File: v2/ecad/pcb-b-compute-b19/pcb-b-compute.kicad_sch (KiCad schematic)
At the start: 925 parts, among them Q1 CSD19532Q5B 100 V N-FET (4.6 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, Q10 2N7002: the changeover's comp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, Q101 BC857: LED_nPWR must be buffe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, Q102 2N7002, Q103 2N7002, Q104 2N7002, Q105 2N7002, Q106 2N7002 EMCON -> W_DISABLE1#, Q2 2N7002 expander -> switch res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, Q201 BC857: LED_nPWR must be buffe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, Q202 2N7002, Q203 2N7002, Q204 2N7002, Q205 2N7002, Q206 2N7002 EMCON -> W_DISABLE1#, Q207 2N7002 expander -> FULL_CARD_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, Q208 2N7002 expander -> RESET#, Q3 2N7002: a voted majority pull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, Q301 BC857: LED_nPWR must be buffe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, Q302 2N7002, Q303 2N7002, Q304 2N7002, Q305 2N7002, Q306 2N7002 EMCON -> W_DISABLE1#, Q4 2N7002: a voted majority pull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, Q5 2N7002: a voted majority pull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, T1 Pulse H5007NL 1000BASE-T magn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, U1 Microchip KSZ9897RTXI seven-p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, U10 TMP117AIDRVR board temperatur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, U101 Diodes PI7C9X2G404SL PCIe 2.0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, U102 TI TUSB8041IRGCR four-port US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, U103 AP64500SP-13 5 A buck, 3.3 V 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, U104 AP64500SP-13 5 A buck, 3.3 V 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, U105 TPS62933DRLR buck 1.0 V PCIe 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, U106 TPS62933DRLR buck 1.1 V hub c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, U107 USBLC6-2SC6, U109 TI TMUXHS4212 SuperSpeed 2:1 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, U11 Quectel LG290P03AAMD GNSS RTK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, U110 TI TS3USB221A USB2 2:1 host s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, U12 Ebyte E22-900M30S 1 W LoRa (S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, U13 Ebyte E72-2G4M20S1E CC2652P (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, U14 Ebyte E72-2G4M20S1E CC2652P (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, U15 CP2102N-A02-GQFN28 USB-UART b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, U16 CP2102N-A02-GQFN28 USB-UART b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, U17 CP2102N-A02-GQFN28 USB-UART b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, U18 CP2102N-A02-GQFN28 USB-UART b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, U19 SN74LVC08APWR quad AND: LimeS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, U20 SN74LVC08APWR quad AND: E72 r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, U201 Diodes PI7C9X2G404SL PCIe 2.0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, U202 TI TUSB8041IRGCR four-port US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, U203 AP64500SP-13 5 A buck, 3.3 V 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, U204 AP64500SP-13 5 A buck, 3.3 V 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, U205 TPS62933DRLR buck 1.0 V PCIe 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, U206 TPS62933DRLR buck 1.1 V hub c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, U207 USBLC6-2SC6, U209 TI TMUXHS4212 SuperSpeed 2:1 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, U21 TPS22810DRV, U210 TI TS3USB221A USB2 2:1 host s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, U22 TPS22810DRV, U23 TPS259631DDAR eFuse +5V_DEV -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, U24 TPS259631DDAR eFuse +5V_DEV -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, U25 AP63203WU-7 3.3 V 2 A buck: t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, U26 TPS62933DRLR buck 1.2 V Ether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, U27 AP2112K-2.5 LDO: the switch's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, U28 TPS2065CDBV, U29 USBLC6-2SC6, U3 TI TS3DV642A0RUAR HDMI 2:1 sw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, U301 Diodes PI7C9X2G404SL PCIe 2.0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, U302 TI TUSB8041IRGCR four-port US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, U303 AP64500SP-13 5 A buck, 3.3 V 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, U304 AP64500SP-13 5 A buck, 3.3 V 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, U305 TPS62933DRLR buck 1.0 V PCIe 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, U306 TPS62933DRLR buck 1.1 V hub c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, U307 USBLC6-2SC6, U309 TI TMUXHS4212 SuperSpeed 2:1 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, U30A Amphenol 10164227-1004A1RLF r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, U30B Amphenol 10164227-1004A1RLF r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, U310 TI TS3USB221A USB2 2:1 host s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, U31A Amphenol 10164227-1004A1RLF r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, U31B Amphenol 10164227-1004A1RLF r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

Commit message: fix(ecad): the six committed netlists came from schematics this tree does not hold [MESHSAT-862]
`sch_prov.py` records the sha256 of the schematic a netlist was generated from,
and on every one of the six boards it named a schematic that is not the one in
the repo: the netlists were regenerated and committed at 00:14 this morning
without their schematics, which are from 15 and 16 September. Board E is the
clearest case, its committed netlist carrying the SMCJ40A and the 100 V bulk
capacitor of the suppressor pass while its committed drawing still showed the
SMCJ33A they replaced.

Only board B tripped the timestamp guard, because only board B's schematic had
been rewritten (with identical content) after the netlist, so the contract gate
refused board B and passed five boards in the identical state. That is a guard
reading a proxy while the fact sits beside it.

- check_contracts compares the sidecar's schematic hash when there is one and
  keeps the mtime rule only for a netlist with no provenance. A rule holds both
  directions and fails on the pre-fix source ("a netlist generated from a
  schematic this tree does not hold was accepted because its mtime is older").
- the six schematics are regenerated by today's generators at each board's own
  declared phase, and each board's netlist was exported from the new schematic
  and compared with the committed one component by component and node by node:
  398/262, 931/1852, 194/144, 207/172, 161/118 and 56/39 components and nets
  agree on every node. No connectivity moved; what moved is the drawing, which
  had been left behind, and E's two part values, which the netlist already had.
  erc_gate PASS on all six.
- the contract gate on this tree now reads PASS of 72 where it read INCONCLUSIVE
  of 54 with 24 contracts unjudged, which is SCH-003 and INT-001 on six boards.

Suite 928 passing, 0 failing, 19 skipped.
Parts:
- removed C121, C223: 22u 10V X7R 1210, Capacitor_SMD:C_1210_3225Metric, symbol Device:C
- removed C218, C237, C238, C239, C240, C250, C266, C267, C268, C269, C289, C60: 100n, Capacitor_SMD:C_0603_1608Metric, symbol Device:C
- removed C229, C234: 10n, Capacitor_SMD:C_0603_1608Metric, symbol Device:C
- removed C231, C232, C249: 22u 6.3V, Capacitor_SMD:C_0805_2012Metric, symbol Device:C
- removed C277, C278, C281, C282, C375, C377, C381: 100n, Capacitor_SMD:C_0402_1005Metric, symbol Device:C
- removed C59: 4.7u, Capacitor_SMD:C_0805_2012Metric, symbol Device:C
- removed J_QMX: QMX USB lead (bank 2 hub, port 4): VBUS D- D+ GND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, Connector_PinHeader_2.54mm:PinHeader_1x04_P2.54mm_Vertical, symbol Connector_Generic:Conn_01x04
- removed L203, L204: 2.2uH XAL4020-222ME, Inductor_SMD:L_Coilcraft_XAL4020-XXX, symbol Device:L
- removed Q302: 2N7002, Package_TO_SOT_SMD:SOT-23, symbol Transistor_FET:2N7002
- removed R138, R245, R346: 10k, Resistor_SMD:R_0603_1608Metric, symbol Device:R
- removed R143: 90.9k 1%, Resistor_SMD:R_0603_1608Metric, symbol Device:R
- removed R150, R40: 1k, Resistor_SMD:R_0603_1608Metric, symbol Device:R
- removed R202: 31.6k 1%, Resistor_SMD:R_0603_1608Metric, symbol Device:R
- removed R205, R210: 22k, Resistor_SMD:R_0603_1608Metric, symbol Device:R
- removed R211, R477, R480, R481, R482, R483, R484: 100k, Resistor_SMD:R_0603_1608Metric, symbol Device:R
- removed R219, R320, R321: 5.1k, Resistor_SMD:R_0603_1608Metric, symbol Device:R
- removed R222, R324: 330, Resistor_SMD:R_0603_1608Metric, symbol Device:R
- removed R242: 9.53k 1%, Resistor_SMD:R_0603_1608Metric, symbol Device:R
- removed U303: AP64500SP-13 5 A buck, 3.3 V rail +3V3_S3A, Package_SO:SOIC-8-1EP_3.9x4.9mm_P1.27mm_EP2.29x3mm, symbol meshsat_ic:U303
- removed U34: USBLC6-2SC6, Package_TO_SOT_SMD:SOT-23-6, symbol Power_Protection:USBLC6-2SC6
- removed U40: AP2112K-3.3 LDO: the private 3.3 V of controller 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, Package_TO_SOT_SMD:SOT-23-5, symbol meshsat_ic:U40
- removed U62: SWD pads, controller C: 3V3 SWDIO SWCLK NRST GND, Connector_PinHeader_2.54mm:PinHeader_1x05_P2.54mm_Vertical, symbol meshsat_ic:U62
- removed U77: SN74LVC32APWR quad 2-input OR: the 2-of-3 majorit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, Package_SO:TSSOP-14_4.4x5mm_P0.65mm, symbol meshsat_ic:U77
- removed U8: ATECC608B-SSHDA-T secure element (I2C 0x60): keys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, Package_SO:SOIC-8_3.9x4.9mm_P1.27mm, symbol meshsat_ic:U8
- added C135, C241, C242, C243, C244, C245, C270, C271, C272, C273, C292, C294, C406, C475, C476, C477, C478, C479, C70: 100n, Capacitor_SMD:C_0603_1608Metric, symbol Device:C
- added C151, C152, C251, C252, C351, C352: 220n 16V (PCIe AC coupling, CM5 datasheet 2.3.1), Capacitor_SMD:C_0402_1005Metric, symbol Device:C
- added C157, C226, C227, C331: 22u 6.3V, Capacitor_SMD:C_0805_2012Metric, symbol Device:C
- added C159, C275, C279: 100n, Capacitor_SMD:C_0402_1005Metric, symbol Device:C
- added C212, C219: 22u 10V X7R 1210, Capacitor_SMD:C_1210_3225Metric, symbol Device:C
- added C225, C230: 10u, Capacitor_SMD:C_0805_2012Metric, symbol Device:C
- added C265: 18p, Capacitor_SMD:C_0402_1005Metric, symbol Device:C
- added C293: 1u, Capacitor_SMD:C_0603_1608Metric, symbol Device:C
- added C61: 10n, Capacitor_SMD:C_0603_1608Metric, symbol Device:C
- added J_FAN1: IP68 cooler fan of S1 (JST-SH 1.0): 5V GND TACHO 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, Connector_JST:JST_SH_BM04B-SRSS-TB_1x04-1MP_P1.00mm_Vertical, symbol Connector_Generic:Conn_01x04
- added L201, L202: 3.3uH XAL6030-332ME, Inductor_SMD:L_Coilcraft_XAL6060-XXX, symbol Device:L
- added LED23, LED33: green card link (PORTSTATUS1), LED_SMD:LED_0603_1608Metric, symbol Device:LED
- added LED26, LED36: green ACT (LED_nACT sinks), LED_SMD:LED_0603_1608Metric, symbol Device:LED
- added LED31: green 5 V S3, LED_SMD:LED_0603_1608Metric, symbol Device:LED
- added Q206: 2N7002 EMCON -> W_DISABLE1#, Package_TO_SOT_SMD:SOT-23, symbol Transistor_FET:2N7002
- added R208: 10k 1%, Resistor_SMD:R_0603_1608Metric, symbol Device:R
- added R214: 40.2k 1%, Resistor_SMD:R_0603_1608Metric, symbol Device:R
- added R216: 26.7k 1%, Resistor_SMD:R_0603_1608Metric, symbol Device:R
- added R230, R330: 1k, Resistor_SMD:R_0603_1608Metric, symbol Device:R
- added R251, R349, R351, R44: 10k, Resistor_SMD:R_0603_1608Metric, symbol Device:R
- added R305: 22k, Resistor_SMD:R_0603_1608Metric, symbol Device:R
- added R328: 330, Resistor_SMD:R_0603_1608Metric, symbol Device:R
- added R43: 301R 1% (ILM: 3.0 A), Resistor_SMD:R_0603_1608Metric, symbol Device:R
- added R478: 100k, Resistor_SMD:R_0603_1608Metric, symbol Device:R
- added U19: SN74LVC08APWR quad AND: LimeSDR (hub port power A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, Package_SO:TSSOP-14_4.4x5mm_P0.65mm, symbol meshsat_ic:U19
- added U29: USBLC6-2SC6, Package_TO_SOT_SMD:SOT-23-6, symbol Power_Protection:USBLC6-2SC6
- added U63: TCAN334D CAN-FD transceiver, controller C on hear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, Package_SO:SOIC-8_3.9x4.9mm_P1.27mm, symbol meshsat_ic:U63
- added U78: SN74LVC32APWR quad 2-input OR: the 2-of-3 majorit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, Package_SO:TSSOP-14_4.4x5mm_P0.65mm, symbol meshsat_ic:U78
- C114: renamed from C157; value 22u 6.3V -> 22u 10V X7R 1210; footprint Capacitor_SMD:C_0805_2012Metric -> Capacitor_SMD:C_1210_3225Metric
- C121: renamed from C135; value 100n -> 22u 10V X7R 1210; footprint Capacitor_SMD:C_0603_1608Metric -> Capacitor_SMD:C_1210_3225Metric
- C218: renamed from R207; value 31.6k 1% -> 100n; footprint Resistor_SMD:R_0603_1608Metric -> Capacitor_SMD:C_0603_1608Metric; symbol Device:R -> Device:C
- C223: renamed from C247; value 10u -> 22u 10V X7R 1210; footprint Capacitor_SMD:C_0805_2012Metric -> Capacitor_SMD:C_1210_3225Metric
- C229: renamed from C225; value 10u -> 10n; footprint Capacitor_SMD:C_0805_2012Metric -> Capacitor_SMD:C_0603_1608Metric
- C231: renamed from C270; value 100n -> 22u 6.3V; footprint Capacitor_SMD:C_0603_1608Metric -> Capacitor_SMD:C_0805_2012Metric
- C232: renamed from C271; value 100n -> 22u 6.3V; footprint Capacitor_SMD:C_0603_1608Metric -> Capacitor_SMD:C_0805_2012Metric
- C234: renamed from C230; value 10u -> 10n; footprint Capacitor_SMD:C_0805_2012Metric -> Capacitor_SMD:C_0603_1608Metric
- C237: renamed from C226; value 22u 6.3V -> 100n; footprint Capacitor_SMD:C_0805_2012Metric -> Capacitor_SMD:C_0603_1608Metric
- C238: renamed from C227; value 22u 6.3V -> 100n; footprint Capacitor_SMD:C_0805_2012Metric -> Capacitor_SMD:C_0603_1608Metric
- C247: renamed from C243; value 100n -> 10u; footprint Capacitor_SMD:C_0603_1608Metric -> Capacitor_SMD:C_0805_2012Metric
- C249: renamed from C244; value 100n -> 22u 6.3V; footprint Capacitor_SMD:C_0603_1608Metric -> Capacitor_SMD:C_0805_2012Metric
- C269: renamed from C293; value 1u -> 100n
- C274: renamed from C294; value 100n -> 10u; footprint Capacitor_SMD:C_0603_1608Metric -> Capacitor_SMD:C_0805_2012Metric
- C276: renamed from LED26; value green ACT (LED_nACT sinks) -> 100n; footprint LED_SMD:LED_0603_1608Metric -> Capacitor_SMD:C_0402_1005Metric; symbol Device:LED -> Device:C; LCSC C12624 -> (none)
- C280: renamed from R251; value 10k -> 100n; footprint Resistor_SMD:R_0603_1608Metric -> Capacitor_SMD:C_0402_1005Metric; symbol Device:R -> Device:C
- C289: renamed from Q206; value 2N7002 EMCON -> W_DISABLE1# -> 100n; footprint Package_TO_SOT_SMD:SOT-23 -> Capacitor_SMD:C_0603_1608Metric; symbol Transistor_FET:2N7002 -> Device:C; LCSC C8545 -> (none)
- C375: renamed from R349; value 10k -> 100n; footprint Resistor_SMD:R_0603_1608Metric -> Capacitor_SMD:C_0402_1005Metric; symbol Device:R -> Device:C
- C377: renamed from LED36; value green ACT (LED_nACT sinks) -> 100n; footprint LED_SMD:LED_0603_1608Metric -> Capacitor_SMD:C_0402_1005Metric; symbol Device:LED -> Device:C; LCSC C12624 -> (none)
- C381: renamed from R351; value 10k -> 100n; footprint Resistor_SMD:R_0603_1608Metric -> Capacitor_SMD:C_0402_1005Metric; symbol Device:R -> Device:C
- C59: renamed from R44; value 10k -> 4.7u; footprint Resistor_SMD:R_0603_1608Metric -> Capacitor_SMD:C_0805_2012Metric; symbol Device:R -> Device:C
- C60: renamed from R43; value 301R 1% (ILM: 3.0 A) -> 100n; footprint Resistor_SMD:R_0603_1608Metric -> Capacitor_SMD:C_0603_1608Metric; symbol Device:R -> Device:C
- D101, D201, D301: value SMBJ5.0A -> SMBJ6.0A (6.0 V standoff on the 5.1 V slot rail); LCSC (none) -> C83270
- J_QMX: renamed from U19; value SN74LVC08APWR quad AND: LimeSDR (hub port power AND EMCON AND software), RockBLOCK (EMCON AND software), LoRa (EMCON AN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 -> QMX USB lead (bank 2 hub, port 4): VBUS D- D+ GND; pigtail to the unit's USB-C; footprint Package_SO:TSSOP-14_4.4x5mm_P0.65mm -> Connector_PinHeader_2.54mm:PinHeader_1x04_P2.54mm_Vertical; symbol meshsat_ic:U19 -> Connector_Generic:Conn_01x04; LCSC C465737 -> (none)
- L203: renamed from R214; value 40.2k 1% -> 2.2uH XAL4020-222ME; footprint Resistor_SMD:R_0603_1608Metric -> Inductor_SMD:L_Coilcraft_XAL4020-XXX; symbol Device:R -> Device:L
- L204: renamed from R216; value 26.7k 1% -> 2.2uH XAL4020-222ME; footprint Resistor_SMD:R_0603_1608Metric -> Inductor_SMD:L_Coilcraft_XAL4020-XXX; symbol Device:R -> Device:L
- Q302: renamed from LED31; value green 5 V S3 -> 2N7002; footprint LED_SMD:LED_0603_1608Metric -> Package_TO_SOT_SMD:SOT-23; symbol Device:LED -> Transistor_FET:2N7002; LCSC C12624 -> C8545
- R138: renamed from C114; value 22u 10V X7R 1210 -> 10k; footprint Capacitor_SMD:C_1210_3225Metric -> Resistor_SMD:R_0603_1608Metric; symbol Device:C -> Device:R
- R143: renamed from C159; value 100n -> 90.9k 1%; footprint Capacitor_SMD:C_0402_1005Metric -> Resistor_SMD:R_0603_1608Metric; symbol Device:C -> Device:R
- R150: renamed from J_FAN1; value IP68 cooler fan of S1 (JST-SH 1.0): 5V GND TACHO PWM -> 1k; footprint Connector_JST:JST_SH_BM04B-SRSS-TB_1x04-1MP_P1.00mm_Vertical -> Resistor_SMD:R_0603_1608Metric; symbol Connector_Generic:Conn_01x04 -> Device:R; LCSC C160390 -> (none)
- R202: renamed from L201; value 3.3uH XAL6030-332ME -> 31.6k 1%; footprint Inductor_SMD:L_Coilcraft_XAL6060-XXX -> Resistor_SMD:R_0603_1608Metric; symbol Device:L -> Device:R
- R205: renamed from C212; value 22u 10V X7R 1210 -> 22k; footprint Capacitor_SMD:C_1210_3225Metric -> Resistor_SMD:R_0603_1608Metric; symbol Device:C -> Device:R
- R207: renamed from L202; value 3.3uH XAL6030-332ME -> 31.6k 1%; footprint Inductor_SMD:L_Coilcraft_XAL6060-XXX -> Resistor_SMD:R_0603_1608Metric; symbol Device:L -> Device:R
- R210: renamed from C219; value 22u 10V X7R 1210 -> 22k; footprint Capacitor_SMD:C_1210_3225Metric -> Resistor_SMD:R_0603_1608Metric; symbol Device:C -> Device:R
- R211: renamed from R208; value 10k 1% -> 100k
- R219: renamed from LED23; value green card link (PORTSTATUS1) -> 5.1k; footprint LED_SMD:LED_0603_1608Metric -> Resistor_SMD:R_0603_1608Metric; symbol Device:LED -> Device:R; LCSC C12624 -> (none)
- R222: renamed from R230; value 1k -> 330
- R242: renamed from C274; value 10u -> 9.53k 1%; footprint Capacitor_SMD:C_0805_2012Metric -> Resistor_SMD:R_0603_1608Metric; symbol Device:C -> Device:R
- R245: renamed from C265; value 18p -> 10k; footprint Capacitor_SMD:C_0402_1005Metric -> Resistor_SMD:R_0603_1608Metric; symbol Device:C -> Device:R
- R320: renamed from R328; value 330 -> 5.1k
- R321: renamed from LED33; value green card link (PORTSTATUS1) -> 5.1k; footprint LED_SMD:LED_0603_1608Metric -> Resistor_SMD:R_0603_1608Metric; symbol Device:LED -> Device:R; LCSC C12624 -> (none)
- R324: renamed from R330; value 1k -> 330
- R346: renamed from C331; value 22u 6.3V -> 10k; footprint Capacitor_SMD:C_0805_2012Metric -> Resistor_SMD:R_0603_1608Metric; symbol Device:C -> Device:R
- R40: renamed from C61; value 10n -> 1k; footprint Capacitor_SMD:C_0603_1608Metric -> Resistor_SMD:R_0603_1608Metric; symbol Device:C -> Device:R
- R480: renamed from C475; value 100n -> 100k; footprint Capacitor_SMD:C_0603_1608Metric -> Resistor_SMD:R_0603_1608Metric; symbol Device:C -> Device:R
- R481: renamed from C476; value 100n -> 100k; footprint Capacitor_SMD:C_0603_1608Metric -> Resistor_SMD:R_0603_1608Metric; symbol Device:C -> Device:R
- R482: renamed from C477; value 100n -> 100k; footprint Capacitor_SMD:C_0603_1608Metric -> Resistor_SMD:R_0603_1608Metric; symbol Device:C -> Device:R
- R483: renamed from C479; value 100n -> 100k; footprint Capacitor_SMD:C_0603_1608Metric -> Resistor_SMD:R_0603_1608Metric; symbol Device:C -> Device:R
- R484: renamed from C478; value 100n -> 100k; footprint Capacitor_SMD:C_0603_1608Metric -> Resistor_SMD:R_0603_1608Metric; symbol Device:C -> Device:R
- U303: renamed from R305; value 22k -> AP64500SP-13 5 A buck, 3.3 V rail +3V3_S3A; footprint Resistor_SMD:R_0603_1608Metric -> Package_SO:SOIC-8-1EP_3.9x4.9mm_P1.27mm_EP2.29x3mm; symbol Device:R -> meshsat_ic:U303; LCSC (none) -> C2070920
- U40: renamed from C406; value 100n -> AP2112K-3.3 LDO: the private 3.3 V of controller A, its own branch off the device rail; footprint Capacitor_SMD:C_0603_1608Metric -> Package_TO_SOT_SMD:SOT-23-5; symbol Device:C -> meshsat_ic:U40
- U62: renamed from U63; value TCAN334D CAN-FD transceiver, controller C on heartbeat fabric A -> SWD pads, controller C: 3V3 SWDIO SWCLK NRST GND; footprint Package_SO:SOIC-8_3.9x4.9mm_P1.27mm -> Connector_PinHeader_2.54mm:PinHeader_1x05_P2.54mm_Vertical; symbol meshsat_ic:U63 -> meshsat_ic:U62; LCSC C2871143 -> (none)
- U77: renamed from U78; symbol meshsat_ic:U78 -> meshsat_ic:U77
- U8: renamed from C70; value 100n -> ATECC608B-SSHDA-T secure element (I2C 0x60): keys behind ZEROIZE; footprint Capacitor_SMD:C_0603_1608Metric -> Package_SO:SOIC-8_3.9x4.9mm_P1.27mm; symbol Device:C -> meshsat_ic:U8; LCSC (none) -> C1518769
- renumbered C241 to C239, C242 to C240, C245 to C250, C272 to C266, C273 to C267, C292 to C268, C276 to C277, C275 to C278, C280 to C281, C279 to C282, R478 to R477, U29 to U34
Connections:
- net +1V0_S2: now also L203.2, C226.1, C227.1, C241.1, C242.1, C243.1, C244.1, C245.1; no longer C237.1, C238.1, C239.1, C240.1, C247.1, C249.1, C250.1
- net +1V1_S2: now also C231.1, C232.1, C266.1, C267.1, C268.1, C269.1, C274.1, L204.2; no longer R242.1
- net +1V1_S3: now also C331.1; no longer R346.1
- net +3V3_CM2: now also R211.1, R251.2; no longer C280.2
- net +3V3_CM3: now also Q302.1 (G), R351.2; no longer C381.2
- net +3V3_DEV: now also R245.2, R346.2, U8.8 (+3V3_DEV), C270.1, C271.1, C272.1, C273.1, C292.1, C293.1, C294.1, C475.1, C476.1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; no longer C231.1, C232.1, C266.1, C267.1, C268.1, C269.1, C274.1, C59.2, J_QMX.14 (+3V3_DEV), R480.1, R481.1, R482.1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
- net +3V3_IOCA: now also U40.5 (+3V3_IOCA), C406.1; no longer U40.1
- net +3V3_IOCC: now also U62.1 (+3V3_IOCC), U63.3 (+3V3_IOCC); no longer U62.3 (+3V3_IOCC)
- net +3V3_S1A: now also R138.2, C157.1; no longer R138.1
- net +3V3_S1B: now also C135.1
- net +3V3_S2A: now also R202.1, L201.2, Q206.1 (G); no longer C289.1 (G), R202.2
- net +3V3_S2B: now also C237.1, C238.1, C239.1, C240.1, C247.1, C249.1, C250.1, R207.1, R219.2, L202.2, R230.1; no longer C218.1, R207.2, R222.1
- net +3V3_S3B: now also R320.2, R321.2, R330.1; no longer R324.1
- net +5V_CAM: now also U34.5 (VBUS)
- net +5V_DEV: now also R143.1, U40.1 (+5V_DEV), U40.3 (+5V_DEV), C230.1; no longer C234.1
- net +5V_S1: now also J_FAN1.1 (Pin_1); no longer R150.1 (Pin_1)
- net +5V_S2: now also C212.1, C219.1, C225.1; no longer C229.1, R205.1, R210.1
- net +5V_S3: now also U303.2 (+5V_S3)
- net 5G_W_DIS_n: now also Q206.2 (S); no longer C289.2 (S)
- net BANK1_UPRX_P: now also C159.1; no longer R143.1
- net BSEL3: now also U77.6 (BSEL3)
- net CAM_DM: now also U34.3 (I/O2), U34.4 (I/O2)
- net CAM_DP: now also U34.1 (I/O1), U34.6 (I/O1)
- net CANH_A: now also U63.7 (CANH_A); no longer U62.7 (CANH_A)
- net CANL_A: now also U63.6 (CANL_A); no longer U62.6 (CANL_A)
- net E22_EN: now also U19.11 (E22_EN); no longer J_QMX.11 (E22_EN)
- net EMCON_HW: now also Q206.3 (D), U19.1 (EMCON_HW), U19.12 (EMCON_HW), U19.9 (EMCON_HW); no longer C289.3 (D), J_QMX.1 (EMCON_HW), J_QMX.12 (EMCON_HW), J_QMX.9 (EMCON_HW)
- net EN33_S2: now also R211.2
- net ETH2_P0_N: now also C276.1; no longer C277.1
- net ETH2_P0_P: now also C275.1; no longer C278.1
- net ETH2_P1_N: now also C278.1
- net ETH2_P1_P: now also C277.1
- net ETH2_P2_N: now also C280.1; no longer C281.1
- net ETH2_P2_P: now also C279.1; no longer C282.1
- net ETH2_P3_N: now also C282.1
- net ETH2_P3_P: now also C281.1
- net ETH3_P0_P: now also C375.1
- net ETH3_P1_P: now also C377.1
- net ETH3_P3_P: now also C381.1
- net FAN_PWM1: now also J_FAN1.4 (Pin_4); no longer R150.4 (Pin_4)
- net FAN_PWM2: now also R251.1; no longer C280.1
- net FAN_PWM3: now also R351.1; no longer C381.1
- net FAN_TACHO1: now also J_FAN1.3 (Pin_3); no longer R150.3 (Pin_3)
- net GND: now also C289.2, C59.2, J_QMX.4 (Pin_4), R222.2, R324.2, U303.7 (GND), U303.9 (GND), U62.5 (GND), U8.4 (GND), C135.2, C157.2, C212.2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; no longer J_QMX.7 (GND), L203.2, L204.2, Q302.1 (K), R138.2, R150.2 (Pin_2), R205.2, R210.2, R211.2, R245.2, R320.2, R346.2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
- net HUB1_VBUS: now also R143.2
- net HUB2_R1: now also R242.1
- net HUB2_SMBUS_n: now also R245.1
- net HUB2_XO: now also C265.1; no longer R245.1
- net HUB3_PWRPOL: now also R346.1
- net HUBRST1_AB: now also U77.10 (HUBRST1_AB)
- net HUBRST1_BC: now also U77.9 (HUBRST1_BC)
- net HUBRST1_CA: now also U77.12 (HUBRST1_CA)
- net HUBRST1_O1: now also U77.13 (HUBRST1_O1), U77.8 (HUBRST1_O1)
- net HUBRST1_VOTE: now also R477.1, U77.11 (HUBRST1_VOTE)
- net HUBRST2_AB: now also U78.1 (HUBRST2_AB); no longer U77.1 (HUBRST2_AB)
- net HUBRST2_BC: now also U78.2 (HUBRST2_BC); no longer U77.2 (HUBRST2_BC)
- net HUBRST2_CA: now also U78.5 (HUBRST2_CA); no longer U77.5 (HUBRST2_CA)
- net HUBRST2_O1: now also U78.3 (HUBRST2_O1), U78.4 (HUBRST2_O1); no longer U77.3 (HUBRST2_O1), U77.4 (HUBRST2_O1)
- net HUBRST2_VOTE: now also R478.1, U78.6 (HUBRST2_VOTE); no longer R477.1, U77.6 (HUBRST2_VOTE)
- net HUBRST3_AB: now also U78.10 (HUBRST3_AB); no longer U77.10 (HUBRST3_AB)
- net HUBRST3_BC: now also U78.9 (HUBRST3_BC); no longer U77.9 (HUBRST3_BC)
- net HUBRST3_CA: now also U78.12 (HUBRST3_CA); no longer U77.12 (HUBRST3_CA)
- net HUBRST3_O1: now also U78.13 (HUBRST3_O1), U78.8 (HUBRST3_O1); no longer U77.13 (HUBRST3_O1), U77.8 (HUBRST3_O1)
- net HUBRST3_VOTE: now also U78.11 (HUBRST3_VOTE); no longer U77.11 (HUBRST3_VOTE)
- new net PCIE1_RXSW_N: C152.1, U101.123 (PETN0)
- new net PCIE1_RXSW_P: C151.1, U101.124 (PETP0)
- new net PCIE2_RXSW_N: C252.1, U201.123 (PETN0)
- new net PCIE2_RXSW_P: C251.1, U201.124 (PETP0)
- new net PCIE3_RXSW_N: C352.1, U301.123 (PETN0)
- new net PCIE3_RXSW_P: C351.1, U301.124 (PETP0)
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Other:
- note added: "220n 16V"
- note added: "SMBJ6.0A"
- note added: "page 1 of 37 MeshSat field kit V2, CERN-OHL-S-2.0 PROTOTYPE, nothing built 2026-09-17"
- note added: "page 10 of 37 MeshSat field kit V2, CERN-OHL-S-2.0 PROTOTYPE, nothing built 2026-09-17"
- note added: "page 11 of 37 MeshSat field kit V2, CERN-OHL-S-2.0 PROTOTYPE, nothing built 2026-09-17"
- note added: "page 12 of 37 MeshSat field kit V2, CERN-OHL-S-2.0 PROTOTYPE, nothing built 2026-09-17"
- note added: "page 13 of 37 MeshSat field kit V2, CERN-OHL-S-2.0 PROTOTYPE, nothing built 2026-09-17"
- note added: "page 14 of 37 MeshSat field kit V2, CERN-OHL-S-2.0 PROTOTYPE, nothing built 2026-09-17"
- note added: "page 15 of 37 MeshSat field kit V2, CERN-OHL-S-2.0 PROTOTYPE, nothing built 2026-09-17"
- note added: "page 16 of 37 MeshSat field kit V2, CERN-OHL-S-2.0 PROTOTYPE, nothing built 2026-09-17"
- note added: "page 17 of 37 MeshSat field kit V2, CERN-OHL-S-2.0 PROTOTYPE, nothing built 2026-09-17"
- note added: "page 18 of 37 MeshSat field kit V2, CERN-OHL-S-2.0 PROTOTYPE, nothing built 2026-09-17"
- note added: "page 19 of 37 MeshSat field kit V2, CERN-OHL-S-2.0 PROTOTYPE, nothing built 2026-09-17"
- note added: "page 2 of 37 MeshSat field kit V2, CERN-OHL-S-2.0 PROTOTYPE, nothing built 2026-09-17"
- note added: "page 20 of 37 MeshSat field kit V2, CERN-OHL-S-2.0 PROTOTYPE, nothing built 2026-09-17"
- note added: "page 21 of 37 MeshSat field kit V2, CERN-OHL-S-2.0 PROTOTYPE, nothing built 2026-09-17"
- note added: "page 22 of 37 MeshSat field kit V2, CERN-OHL-S-2.0 PROTOTYPE, nothing built 2026-09-17"
- note added: "page 23 of 37 MeshSat field kit V2, CERN-OHL-S-2.0 PROTOTYPE, nothing built 2026-09-17"
- note added: "page 24 of 37 MeshSat field kit V2, CERN-OHL-S-2.0 PROTOTYPE, nothing built 2026-09-17"
- note added: "page 25 of 37 MeshSat field kit V2, CERN-OHL-S-2.0 PROTOTYPE, nothing built 2026-09-17"
- note added: "page 26 of 37 MeshSat field kit V2, CERN-OHL-S-2.0 PROTOTYPE, nothing built 2026-09-17"
- note added: "page 27 of 37 MeshSat field kit V2, CERN-OHL-S-2.0 PROTOTYPE, nothing built 2026-09-17"
- note added: "page 28 of 37 MeshSat field kit V2, CERN-OHL-S-2.0 PROTOTYPE, nothing built 2026-09-17"
- note added: "page 29 of 37 MeshSat field kit V2, CERN-OHL-S-2.0 PROTOTYPE, nothing built 2026-09-17"
- note added: "page 3 of 37 MeshSat field kit V2, CERN-OHL-S-2.0 PROTOTYPE, nothing built 2026-09-17"
- note added: "page 30 of 37 MeshSat field kit V2, CERN-OHL-S-2.0 PROTOTYPE, nothing built 2026-09-17"
- note added: "page 31 of 37 MeshSat field kit V2, CERN-OHL-S-2.0 PROTOTYPE, nothing built 2026-09-17"
- note added: "page 32 of 37 MeshSat field kit V2, CERN-OHL-S-2.0 PROTOTYPE, nothing built 2026-09-17"
- note added: "page 33 of 37 MeshSat field kit V2, CERN-OHL-S-2.0 PROTOTYPE, nothing built 2026-09-17"
- note added: "page 34 of 37 MeshSat field kit V2, CERN-OHL-S-2.0 PROTOTYPE, nothing built 2026-09-17"
- note added: "page 35 of 37 MeshSat field kit V2, CERN-OHL-S-2.0 PROTOTYPE, nothing built 2026-09-17"
- note added: "page 36 of 37 MeshSat field kit V2, CERN-OHL-S-2.0 PROTOTYPE, nothing built 2026-09-17"
- note added: "page 37 of 37 MeshSat field kit V2, CERN-OHL-S-2.0 PROTOTYPE, nothing built 2026-09-17"
- note added: "page 4 of 37 MeshSat field kit V2, CERN-OHL-S-2.0 PROTOTYPE, nothing built 2026-09-17"
- note added: "page 5 of 37 MeshSat field kit V2, CERN-OHL-S-2.0 PROTOTYPE, nothing built 2026-09-17"
- note added: "page 6 of 37 MeshSat field kit V2, CERN-OHL-S-2.0 PROTOTYPE, nothing built 2026-09-17"
- note added: "page 7 of 37 MeshSat field kit V2, CERN-OHL-S-2.0 PROTOTYPE, nothing built 2026-09-17"
- note added: "page 8 of 37 MeshSat field kit V2, CERN-OHL-S-2.0 PROTOTYPE, nothing built 2026-09-17"
- note added: "page 9 of 37 MeshSat field kit V2, CERN-OHL-S-2.0 PROTOTYPE, nothing built 2026-09-17"
- note removed: "page 1 of 37 MeshSat field kit V2, CERN-OHL-S-2.0 PROTOTYPE, nothing built 2026-09-15"
- note removed: "page 10 of 37 MeshSat field kit V2, CERN-OHL-S-2.0 PROTOTYPE, nothing built 2026-09-15"
- note removed: "page 11 of 37 MeshSat field kit V2, CERN-OHL-S-2.0 PROTOTYPE, nothing built 2026-09-15"
- note removed: "page 12 of 37 MeshSat field kit V2, CERN-OHL-S-2.0 PROTOTYPE, nothing built 2026-09-15"
- note removed: "page 13 of 37 MeshSat field kit V2, CERN-OHL-S-2.0 PROTOTYPE, nothing built 2026-09-15"
- note removed: "page 14 of 37 MeshSat field kit V2, CERN-OHL-S-2.0 PROTOTYPE, nothing built 2026-09-15"
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
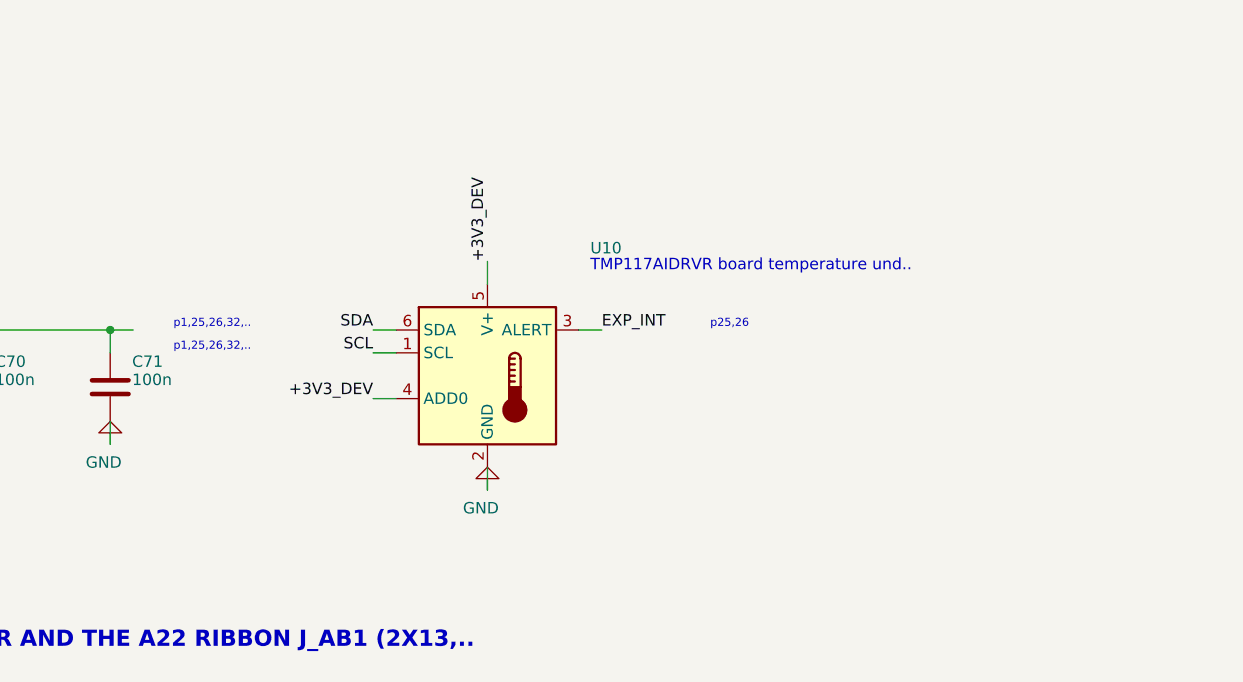
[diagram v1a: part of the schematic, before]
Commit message: fix(ecad): the six netlists regenerated under tonight's engine, with their provenance committed beside them [MESHSAT-862]
kisch.py changed tonight (every map judged against its land and its symbol), so
every committed netlist's sidecar named an older generator and the contract gate
refused to judge the set. Regenerated on the hub at each board's declared phase:
A, C, D and P come back IDENTICAL on every connectivity line (2316, 1067, 1193,
295); B differs by U10's seven pins, E by Q7's five, which are the two design
corrections of 32.219. Board E's board now reads 4 of 818 comparisons behind its
design (Q7) and board B19's 13 of 6735 (U10 and the twelve PCIe receive nets B21
carries), both SCH-002 FAIL and both true.

The sidecars were gitignored with the rest of out/, so every clone had six
netlists with no identity and the gate fell back to the mtime rule that refused one
board and passed five in the identical state this morning; they are force-added and
a rule keeps them beside their netlists. check_contracts reads PASS of 72 on this
tree. Readiness 58.1 percent verified, 11.1 failed, 30.8 inconclusive of 334.
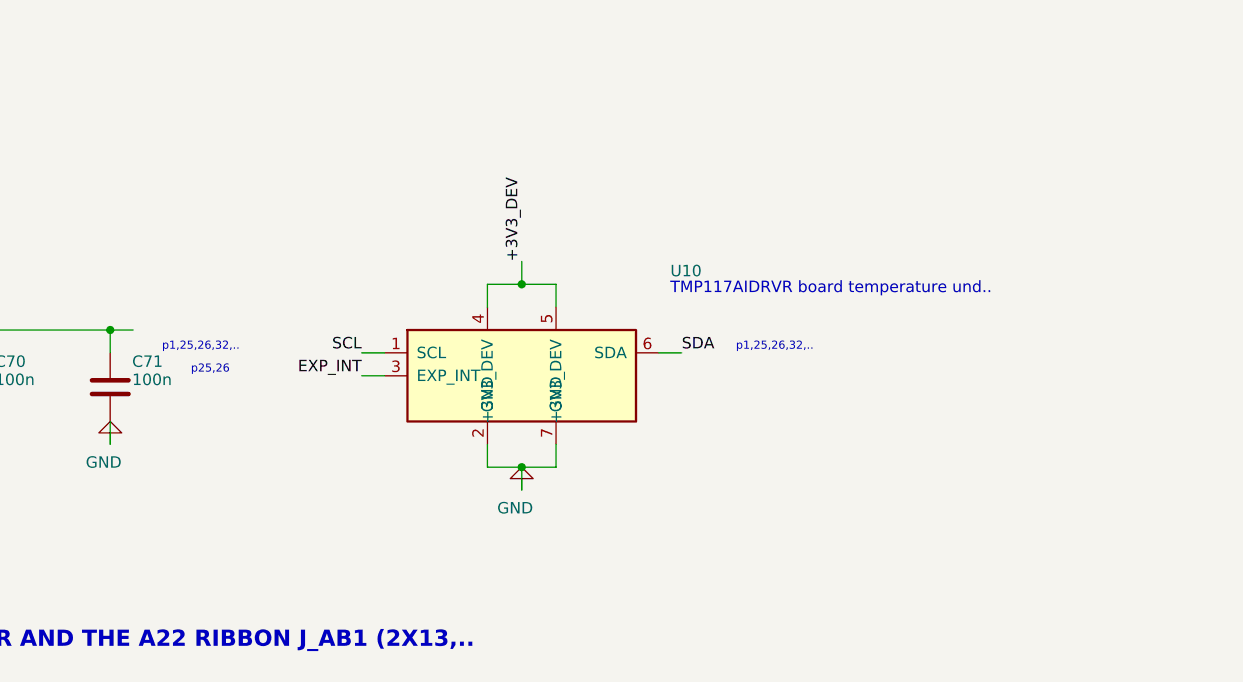
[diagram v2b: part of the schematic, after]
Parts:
- removed R483: 100k, Resistor_SMD:R_0603_1608Metric, symbol Device:R
- added C470: 100n, Capacitor_SMD:C_0603_1608Metric, symbol Device:C
- R483: renamed from C470; value 100n -> 100k; footprint Capacitor_SMD:C_0603_1608Metric -> Resistor_SMD:R_0603_1608Metric; symbol Device:C -> Device:R
- U10: value TMP117AIDRVR board temperature under the coolers (I2C 0x49) -> TMP117AIDRVR board temperature under the coolers (I2C 0x49; WSON-6: 1 SCL 2 GND 3 ALERT 4 V+ 5 ADD0 6 SDA 7 thermal pad); symbol Sensor_Temperature:TMP117xxDRV -> meshsat_ic:U10
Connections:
- net +3V3_DEV: now also C470.1; no longer R483.1
- net GND: now also U10.7 (GND), C470.2
- net SEL2_A: now also R483.1
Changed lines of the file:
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@@
 	(wire (pts (xy 114.30 1623.06) (xy 114.30 1625.60)) (stroke (width 0) (type default)))
 	(wire (pts (xy 114.30 1633.22) (xy 114.30 1635.76)) (stroke (width 0) (type default)))
-	(symbol (lib_id "Sensor_Temperature:TMP117xxDRV") (at 156.21 1628.14 0) (unit 1) (exclude_from_sim no) (in_bom yes) (on_board yes) (dnp no)
-		(property "Reference" "U10" (at 167.64 1614.70 0) (effects (font (size 1.27 1.27)) (justify left bottom)))
-		(property "Value" "TMP117AIDRVR board temperature under the coolers (I2C 0x49)" (at 167.64 1616.71 0) (effects (font (size 1.27 1.27)) (justify left bottom) (hide yes)))
-		(property "Footprint" "Package_SON:WSON-6-1EP_2x2mm_P0.65mm_EP1x1.6mm" (at 156.21 1628.14 0) (effects (font (size 1.27 1.27)) (justify left bottom) (hide yes)))
-		(property "Datasheet" "" (at 156.21 1628.14 0) (effects (font (size 1.27 1.27)) (justify left bottom) (hide yes)))
-		(property "Description" "" (at 156.21 1628.14 0) (effects (font (size 1.27 1.27)) (justify left bottom) (hide yes)))
-		(property "LCSC" "C699536" (at 156.21 1628.14 0) (effects (font (size 1.27 1.27)) (justify left bottom) (hide yes)))
+	(symbol (lib_id "meshsat_ic:U10") (at 160.02 1628.14 0) (unit 1) (exclude_from_sim no) (in_bom yes) (on_board yes) (dnp no)
+		(property "Reference" "U10" (at 176.53 1617.24 0) (effects (font (size 1.27 1.27)) (justify left bottom)))
+		(property "Value" "TMP117AIDRVR board temperature under the coolers (I2C 0x49; WSON-6: 1 SCL 2 GND 3 ALERT 4 V+ 5 ADD0 6 SDA 7 thermal pad)" (at 176.53 1619.25 0) (effects (font (size 1.27 1.27)) (justify left bottom) (hide yes)))
+		(property "Footprint" "Package_SON:WSON-6-1EP_2x2mm_P0.65mm_EP1x1.6mm" (at 160.02 1628.14 0) (effects (font (size 1.27 1.27)) (justify left bottom) (hide yes)))
+		(property "Datasheet" "" (at 160.02 1628.14 0) (effects (font (size 1.27 1.27)) (justify left bottom) (hide yes)))
+		(property "Description" "" (at 160.02 1628.14 0) (effects (font (size 1.27 1.27)) (justify left bottom) (hide yes)))
+		(property "LCSC" "C699536" (at 160.02 1628.14 0) (effects (font (size 1.27 1.27)) (justify left bottom) (hide yes)))
+		(pin "1")
+		(pin "3")
 		(pin "6")
-		(pin "1")
 		(pin "4")
 		(pin "5")
 		(pin "2")
-		(pin "3")
+		(pin "7")
 		(instances (project "pcb-b-compute" (path "/bd4709bc-fac9-5298-bbf9-aec18618ba11" (reference "U10") (unit 1))))
 	)
-	(text "TMP117AIDRVR board temperature und.." (exclude_from_sim no) (at 167.64 1616.71 0) (effects (font (size 1.27 1.27)) (justify left bottom)))
-	(label "SDA" (at 143.51 1623.06 180) (fields_autoplaced yes) (effects (font (size 1.27 1.27)) (justify right bottom)))
-	(label "SCL" (at 143.51 1625.60 180) (fields_autoplaced yes) (effects (font (size 1.27 1.27)) (justify right bottom)))
-	(label "+3V3_DEV" (at 143.51 1630.68 180) (fields_autoplaced yes) (effects (font (size 1.27 1.27)) (justify right bottom)))
-	(label "EXP_INT" (at 168.91 1623.06 0) (fields_autoplaced yes) (effects (font (size 1.27 1.27)) (justify left bottom)))
-	(label "+3V3_DEV" (at 156.21 1615.44 90) (fields_autoplaced yes) (effects (font (size 1.27 1.27)) (justify left bottom)))
-	(symbol (lib_id "power:GND") (at 156.21 1640.84 180) (unit 1) (exclude_from_sim no) (in_bom no) (on_board no) (dnp no) (fields_autoplaced yes)
-		(property "Reference" "#PWR386" (at 157.48 1639.57 0) (effects (font (size 1.27 1.27)) (justify left bottom) (hide yes)))
-		(property "Value" "GND" (at 157.48 1642.11 0) (effects (font (size 1.27 1.27)) (justify left bottom)))
-		(property "Footprint" "" (at 156.21 1640.84 0) (effects (font (size 1.27 1.27)) (justify left bottom) (hide yes)))
-		(property "Datasheet" "" (at 156.21 1640.84 0) (effects (font (size 1.27 1.27)) (justify left bottom) (hide yes)))
-		(property "Description" "" (at 156.21 1640.84 0) (effects (font (size 1.27 1.27)) (justify left bottom) (hide yes)))
+	(text "TMP117AIDRVR board temperature und.." (exclude_from_sim no) (at 176.53 1619.25 0) (effects (font (size 1.27 1.27)) (justify left bottom)))
+	(label "SCL" (at 142.24 1625.60 180) (fields_autoplaced yes) (effects (font (size 1.27 1.27)) (justify right bottom)))
+	(label "EXP_INT" (at 142.24 1628.14 180) (fields_autoplaced yes) (effects (font (size 1.27 1.27)) (justify right bottom)))
+	(label "SDA" (at 177.80 1625.60 0) (fields_autoplaced yes) (effects (font (size 1.27 1.27)) (justify left bottom)))
+	(label "+3V3_DEV" (at 160.02 1615.44 90) (fields_autoplaced yes) (effects (font (size 1.27 1.27)) (justify left bottom)))
+	(symbol (lib_id "power:GND") (at 160.02 1640.84 180) (unit 1) (exclude_from_sim no) (in_bom no) (on_board no) (dnp no) (fields_autoplaced yes)
+		(property "Reference" "#PWR386" (at 161.29 1639.57 0) (effects (font (size 1.27 1.27)) (justify left bottom) (hide yes)))
+		(property "Value" "GND" (at 161.29 1642.11 0) (effects (font (size 1.27 1.27)) (justify left bottom)))
+		(property "Footprint" "" (at 160.02 1640.84 0) (effects (font (size 1.27 1.27)) (justify left bottom) (hide yes)))
+		(property "Datasheet" "" (at 160.02 1640.84 0) (effects (font (size 1.27 1.27)) (justify left bottom) (hide yes)))
+		(property "Description" "" (at 160.02 1640.84 0) (effects (font (size 1.27 1.27)) (justify left bottom) (hide yes)))
 		(pin "1")
 		(instances (project "pcb-b-compute" (path "/bd4709bc-fac9-5298-bbf9-aec18618ba11" (reference "#PWR386") (unit 1))))
 	)
-	(wire (pts (xy 146.05 1623.06) (xy 143.51 1623.06)) (stroke (width 0) (type default)))
-	(wire (pts (xy 146.05 1625.60) (xy 143.51 1625.60)) (stroke (width 0) (type default)))
-	(wire (pts (xy 146.05 1630.68) (xy 143.51 1630.68)) (stroke (width 0) (type default)))
-	(wire (pts (xy 166.37 1623.06) (xy 168.91 1623.06)) (stroke (width 0) (type default)))
-	(wire (pts (xy 156.21 1617.98) (xy 156.21 1615.44)) (stroke (width 0) (type default)))
-	(wire (pts (xy 156.21 1638.30) (xy 156.21 1640.84)) (stroke (width 0) (type default)))
+	(junction (at 160.02 1617.98) (diameter 0) (color 0 0 0 0))
+	(junction (at 160.02 1638.30) (diameter 0) (color 0 0 0 0))
+	(wire (pts (xy 144.78 1625.60) (xy 142.24 1625.60)) (stroke (width 0) (type default)))
+	(wire (pts (xy 144.78 1628.14) (xy 142.24 1628.14)) (stroke (width 0) (type default)))
+	(wire (pts (xy 175.26 1625.60) (xy 177.80 1625.60)) (stroke (width 0) (type default)))
+	(wire (pts (xy 156.21 1620.52) (xy 156.21 1617.98)) (stroke (width 0) (type default)))
+	(wire (pts (xy 163.83 1620.52) (xy 163.83 1617.98)) (stroke (width 0) (type default)))
+	(wire (pts (xy 156.21 1617.98) (xy 160.02 1617.98)) (stroke (width 0) (type default)))
+	(wire (pts (xy 160.02 1617.98) (xy 163.83 1617.98)) (stroke (width 0) (type default)))
+	(wire (pts (xy 160.02 1617.98) (xy 160.02 1615.44)) (stroke (width 0) (type default)))
+	(wire (pts (xy 156.21 1635.76) (xy 156.21 1638.30)) (stroke (width 0) (type default)))
+	(wire (pts (xy 163.83 1635.76) (xy 163.83 1638.30)) (stroke (width 0) (type default)))
+	(wire (pts (xy 156.21 1638.30) (xy 160.02 1638.30)) (stroke (width 0) (type default)))
+	(wire (pts (xy 160.02 1638.30) (xy 163.83 1638.30)) (stroke (width 0) (type default)))
+	(wire (pts (xy 160.02 1638.30) (xy 160.02 1640.84)) (stroke (width 0) (type default)))
 	(symbol (lib_id "Connector_Generic:Conn_02x13_Odd_Even") (at 36.83 1684.02 0) (unit 1) (exclude_from_sim no) (in_bom yes) (on_board yes) (dnp no)
 		(property "Reference" "J_PANEL" (at 45.72 1664.23 0) (effects (font (size 1.27 1.27)) (justify left bottom)))
@@
 	(text "p1,25,26,32,.." (exclude_from_sim no) (at 235.26 1530.25 0) (effects (font (size 0.90 0.90)) (justify left bottom)))
 	(text "p1,25,26,32,.." (exclude_from_sim no) (at 63.17 1622.96 0) (effects (font (size 0.90 0.90)) (justify left bottom)))
-	(text "p1,25,26,32,.." (exclude_from_sim no) (at 121.32 1622.96 0) (effects (font (size 0.90 0.90)) (justify left bottom)))
-	(text "p1,25,26,32,.." (exclude_from_sim no) (at 121.32 1625.50 0) (effects (font (size 0.90 0.90)) (justify left bottom)))
-	(text "p25,26" (exclude_from_sim no) (at 180.96 1622.96 0) (effects (font (size 0.90 0.90)) (justify left bottom)))
+	(text "p1,25,26,32,.." (exclude_from_sim no) (at 120.05 1625.50 0) (effects (font (size 0.90 0.90)) (justify left bottom)))
+	(text "p25,26" (exclude_from_sim no) (at 123.26 1628.04 0) (effects (font (size 0.90 0.90)) (justify left bottom)))
+	(text "p1,25,26,32,.." (exclude_from_sim no) (at 183.82 1625.50 0) (effects (font (size 0.90 0.90)) (justify left bottom)))
 	(text "p8" (exclude_from_sim no) (at 11.84 1686.46 0) (effects (font (size 0.90 0.90)) (justify left bottom)))
 	(text "p17,32,33,34" (exclude_from_sim no) (at 9.33 1691.54 0) (effects (font (size 0.90 0.90)) (justify left bottom)))
